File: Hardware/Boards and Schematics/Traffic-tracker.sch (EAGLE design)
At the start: 7 parts, among them J1 POWER_JACK1

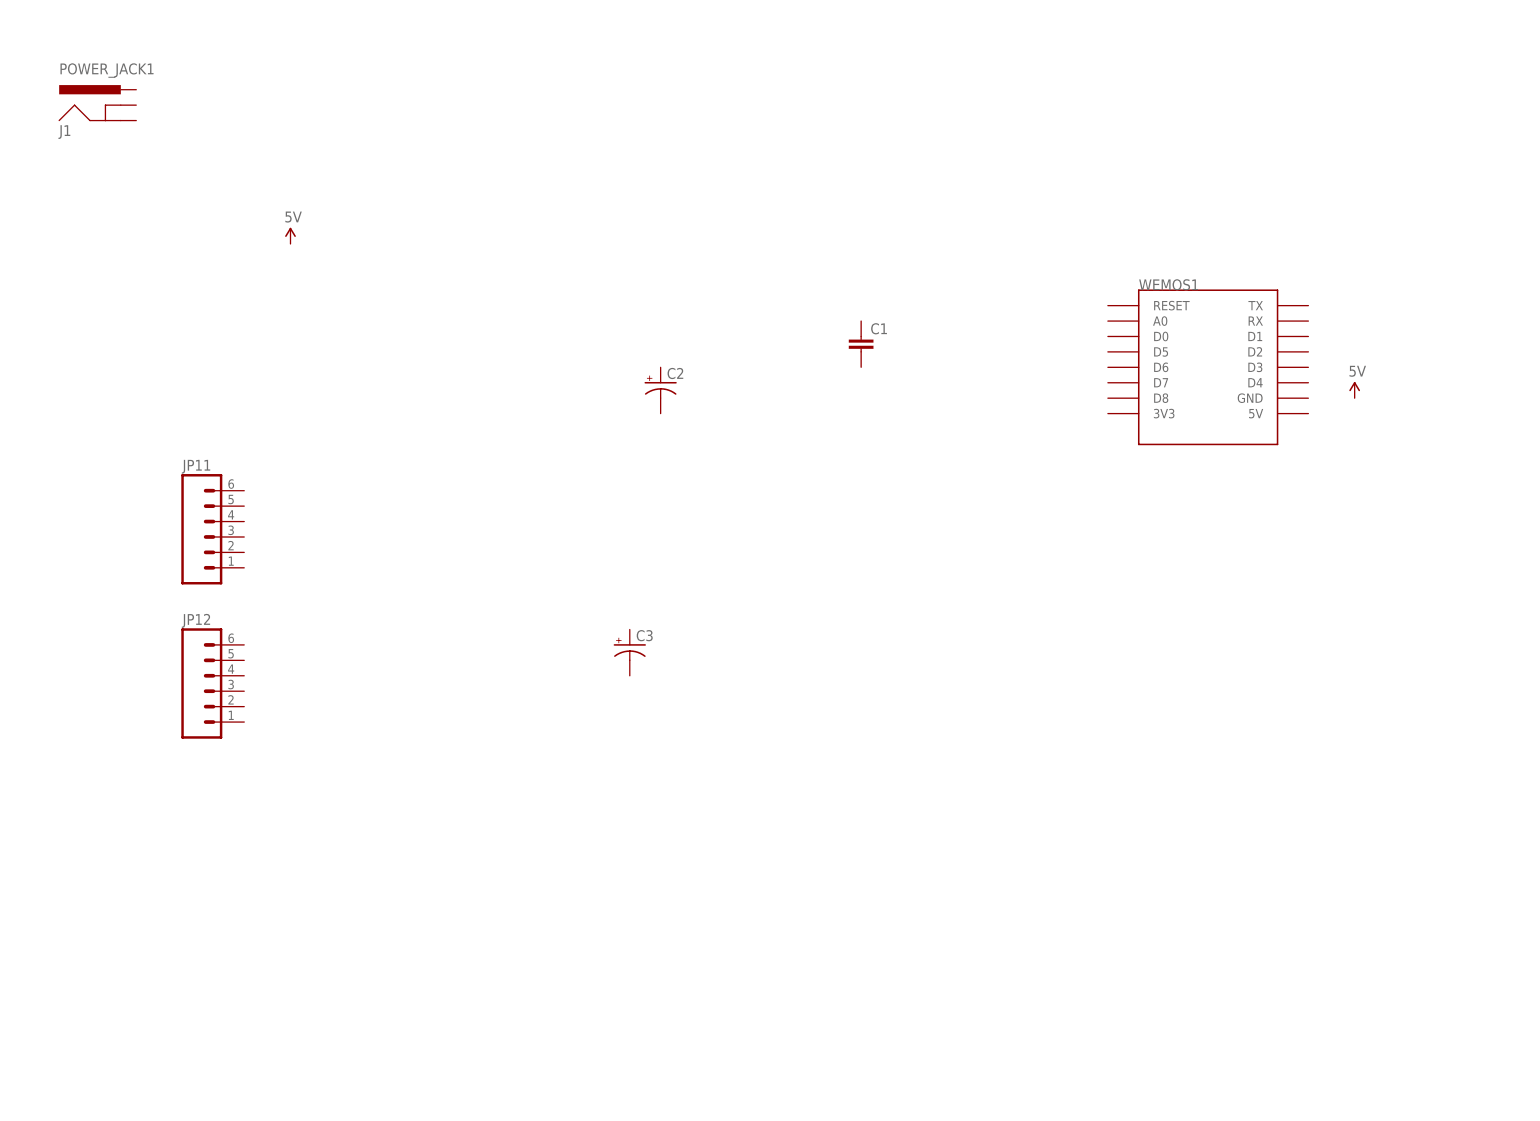
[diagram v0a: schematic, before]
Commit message: Cleaned up schematic, generated and laid out board
Added a 2,2mm barrel jack, 3 pos jumper (for neopixel connection), and
logic level shifter (74AHCT245). Organised schematic neatly.

Board file generated, barrel jack connections double checked, big-ass
trace for 4A connection to neopixels routed. Tried to keep wifi antenna
away from big-ass power traces.

Double checked logic level shifter connections.
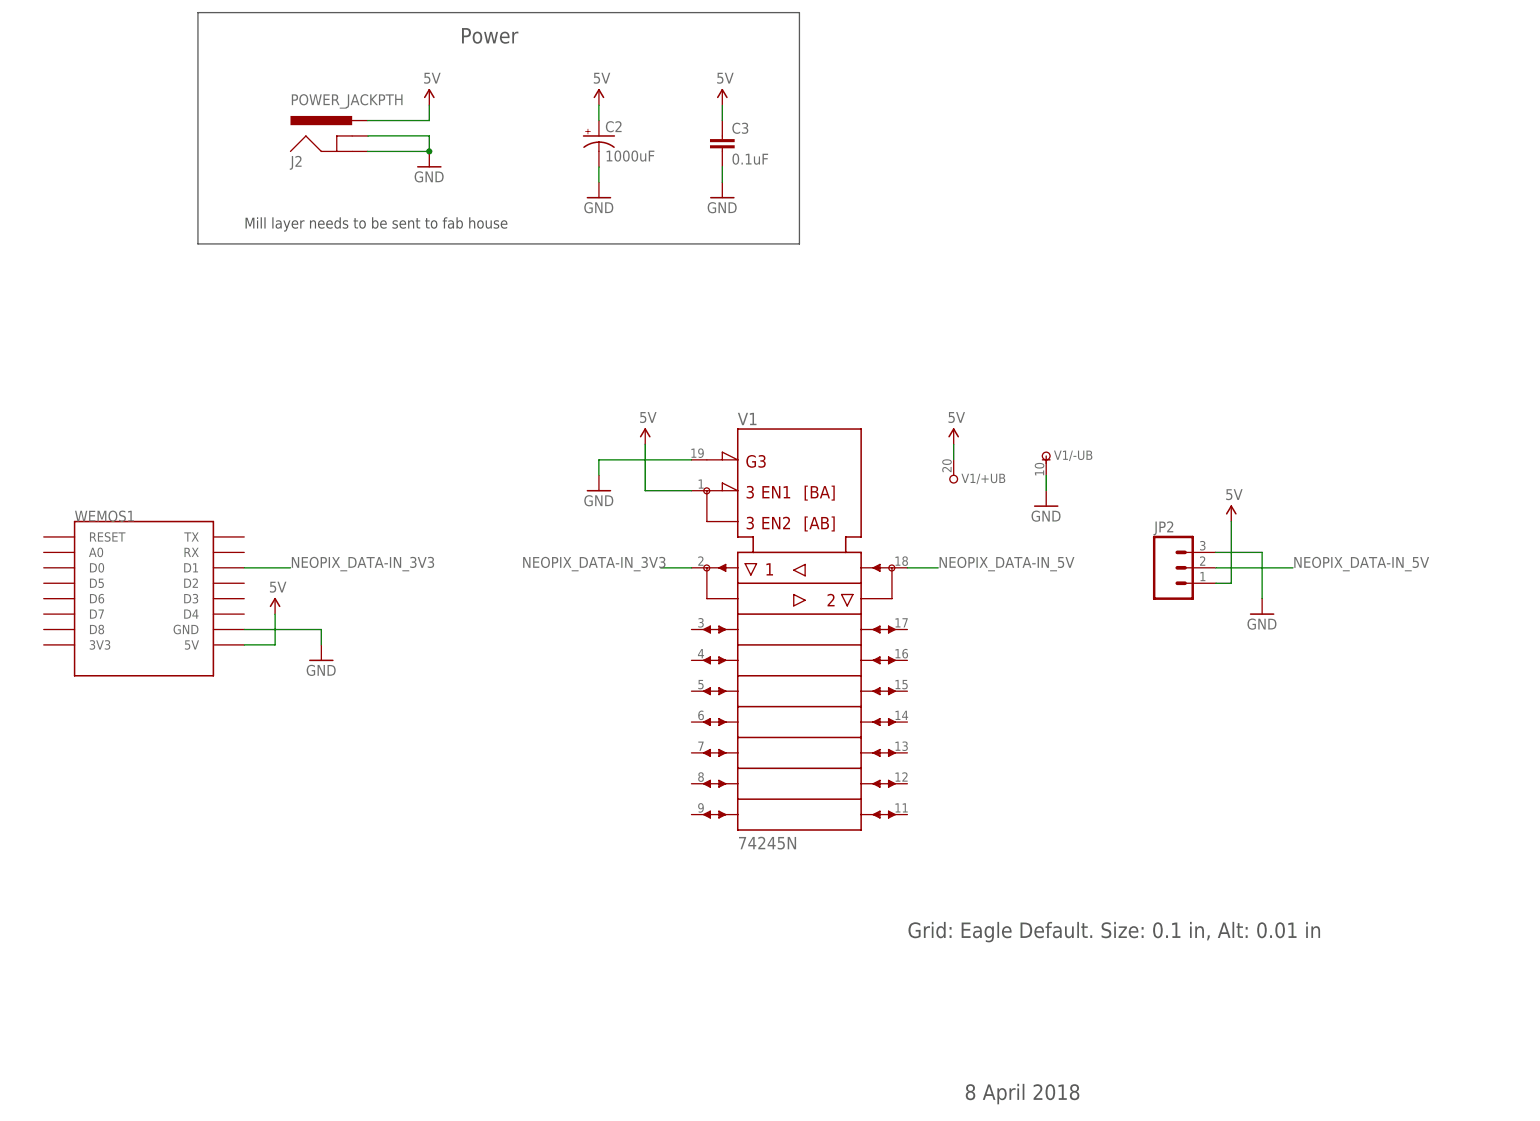
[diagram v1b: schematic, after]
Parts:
- removed C1: (no value), SparkFun:CAP0603-CAP
- removed J1: POWER_JACK1, SparkFun-Connectors:POWER_JACK1
- removed JP11, JP12: (no value), SparkFun-Connectors:M06LOCK
- added J2: POWER_JACKPTH, SparkFun:POWER_JACKPTH
- added JP2: (no value), SparkFun:M03-SCREW-5MM
- added V1: 74245N, 74ttl-din:74245N
- C2: value (none) -> 1000uF
- C3: value (none) -> 0.1uF; device SparkFun-Capacitors:CAP_POLPTH4 -> SparkFun:CAP0603-CAP
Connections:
- new net 5V: C2.+, C3.1, J2.PWR, JP2.1, V1/+UB.+UB, V11.DIR, WEMOS1.5V
- new net GND: C2.-, C3.2, J2.GND, J2.GNDBREAK, JP2.3, V1/-UB.-UB, V11.!G, WEMOS1.GND
- new net NEOPIX_DATA-IN_3V3: V11.A1, WEMOS1.D1
- new net NEOPIX_DATA-IN_5V: JP2.2, V11.B1
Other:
- note added: "8 April 2018"
- note added: "Grid: Eagle Default. Size: 0.1 in, Alt: 0.01 in"
- note added: "Mill layer needs to be sent to fab house"
- note added: "Power"
- moved on the sheet: C2, WEMOS1
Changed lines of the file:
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@@
 <parts>
 <part name="FRAME1" library="frames" deviceset="LETTER_L" device=""/>
-<part name="J1" library="SparkFun-Connectors" deviceset="POWER_JACK" device="1"/>
 <part name="WEMOS1" library="esp8266modules" deviceset="WEMOS-D1-MINI" device=""/>
-<part name="C1" library="SparkFun" deviceset="CAP" device="0603-CAP"/>
-<part name="C2" library="SparkFun-Capacitors" deviceset="CAP_POL" device="PTH4"/>
-<part name="C3" library="SparkFun-Capacitors" deviceset="CAP_POL" device="PTH4"/>
-<part name="JP11" library="SparkFun-Connectors" deviceset="M06" device="LOCK"/>
-<part name="JP12" library="SparkFun-Connectors" deviceset="M06" device="LOCK"/>
+<part name="C2" library="SparkFun-Capacitors" deviceset="CAP_POL" device="PTH4" value="1000uF"/>
 <part name="U$1" library="SparkFun" deviceset="5V" device=""/>
 <part name="U$2" library="SparkFun" deviceset="5V" device=""/>
+<part name="J2" library="SparkFun" deviceset="POWER_JACK" device="PTH"/>
+<part name="GND1" library="SparkFun" deviceset="GND" device=""/>
+<part name="U$4" library="SparkFun" deviceset="5V" device=""/>
+<part name="GND3" library="SparkFun" deviceset="GND" device=""/>
+<part name="GND4" library="SparkFun" deviceset="GND" device=""/>
+<part name="V1" library="74ttl-din" deviceset="74*245" device="N"/>
+<part name="C3" library="SparkFun" deviceset="CAP" device="0603-CAP" value="0.1uF"/>
+<part name="U$5" library="SparkFun" deviceset="5V" device=""/>
+<part name="GND5" library="SparkFun" deviceset="GND" device=""/>
+<part name="U$6" library="SparkFun" deviceset="5V" device=""/>
+<part name="GND6" library="SparkFun" deviceset="GND" device=""/>
+<part name="GND7" library="SparkFun" deviceset="GND" device=""/>
+<part name="U$7" library="SparkFun" deviceset="5V" device=""/>
+<part name="JP2" library="SparkFun" deviceset="M03" device="-SCREW-5MM"/>
+<part name="U$8" library="SparkFun" deviceset="5V" device=""/>
+<part name="GND8" library="SparkFun" deviceset="GND" device=""/>
 </parts>
 <sheets>
 <sheet>
 <plain>
+<text x="40.64" y="144.78" size="1.778" layer="97">Mill layer needs to be sent to fab house</text>
+<wire x1="33.02" y1="180.34" x2="33.02" y2="142.24" width="0.1524" layer="97"/>
+<wire x1="33.02" y1="142.24" x2="132.08" y2="142.24" width="0.1524" layer="97"/>
+<wire x1="132.08" y1="142.24" x2="132.08" y2="180.34" width="0.1524" layer="97"/>
+<wire x1="132.08" y1="180.34" x2="33.02" y2="180.34" width="0.1524" layer="97"/>
+<text x="76.2" y="175.26" size="2.54" layer="97">Power</text>
+<text x="159.258" y="1.27" size="2.54" layer="97">8 April 2018</text>
+<text x="149.86" y="27.94" size="2.54" layer="97">Grid: Eagle Default. Size: 0.1 in, Alt: 0.01 in</text>
 </plain>
 <instances>
 <instance part="FRAME1" gate="G$1" x="0" y="0"/>
-<instance part="FRAME1" gate="G$2" x="147.32" y="0"/>
-<instance part="J1" gate="G$1" x="20.32" y="160.02"/>
-<instance part="WEMOS1" gate="D1" x="198.12" y="121.92"/>
-<instance part="C1" gate="G$1" x="142.24" y="124.46"/>
-<instance part="C2" gate="G$1" x="109.22" y="119.38"/>
-<instance part="C3" gate="G$1" x="104.14" y="76.2"/>
-<instance part="JP11" gate="G$1" x="35.56" y="93.98"/>
-<instance part="JP12" gate="G$1" x="35.56" y="68.58"/>
-<instance part="U$1" gate="G$1" x="223.52" y="116.84"/>
-<instance part="U$2" gate="G$1" x="48.26" y="142.24"/>
+<instance part="FRAME1" gate="G$2" x="147.32" y="0" smashed="yes">
+<attribute name="SHEET" x="233.68" y="1.27" size="2.54" layer="94"/>
+<attribute name="DRAWING_NAME" x="165.1" y="19.05" size="2.54" layer="94"/>
+</instance>
+<instance part="WEMOS1" gate="D1" x="22.86" y="83.82"/>
+<instance part="C2" gate="G$1" x="99.06" y="160.02"/>
+<instance part="U$1" gate="G$1" x="45.72" y="81.28"/>
+<instance part="U$2" gate="G$1" x="71.12" y="165.1"/>
+<instance part="J2" gate="G$1" x="58.42" y="154.94"/>
+<instance part="GND1" gate="1" x="71.12" y="154.94"/>
+<instance part="U$4" gate="G$1" x="99.06" y="165.1"/>
+<instance part="GND3" gate="1" x="99.06" y="149.86"/>
+<instance part="GND4" gate="1" x="53.34" y="73.66"/>
+<instance part="V1" gate="1" x="132.08" y="78.74"/>
+<instance part="C3" gate="G$1" x="119.38" y="157.48"/>
+<instance part="U$5" gate="G$1" x="119.38" y="165.1"/>
+<instance part="GND5" gate="1" x="119.38" y="149.86"/>
+<instance part="V1" gate="/+UB" x="157.48" y="104.14"/>
+<instance part="V1" gate="/-UB" x="172.72" y="106.68"/>
+<instance part="U$6" gate="G$1" x="157.48" y="109.22"/>
+<instance part="GND6" gate="1" x="172.72" y="99.06"/>
+<instance part="GND7" gate="1" x="99.06" y="101.6"/>
+<instance part="U$7" gate="G$1" x="106.68" y="109.22"/>
+<instance part="JP2" gate="G$1" x="193.04" y="88.9"/>
+<instance part="U$8" gate="G$1" x="203.2" y="96.52"/>
+<instance part="GND8" gate="1" x="208.28" y="81.28"/>
 </instances>
 <busses>
 </busses>
 <nets>
+<net name="5V" class="0">
+<segment>
+<pinref part="U$2" gate="G$1" pin="5V"/>
+<wire x1="71.12" y1="165.1" x2="71.12" y2="162.56" width="0.1524" layer="91"/>
+<pinref part="J2" gate="G$1" pin="PWR"/>
+<wire x1="71.12" y1="162.56" x2="60.96" y2="162.56" width="0.1524" layer="91"/>
+</segment>
+<segment>
+<pinref part="U$4" gate="G$1" pin="5V"/>
+<pinref part="C2" gate="G$1" pin="+"/>
+<wire x1="99.06" y1="165.1" x2="99.06" y2="162.56" width="0.1524" layer="91"/>
+</segment>
+<segment>
+<pinref part="U$1" gate="G$1" pin="5V"/>
+<wire x1="45.72" y1="81.28" x2="45.72" y2="76.2" width="0.1524" layer="91"/>
+<pinref part="WEMOS1" gate="D1" pin="5V"/>
+<wire x1="45.72" y1="76.2" x2="40.64" y2="76.2" width="0.1524" layer="91"/>
+</segment>
+<segment>
+<pinref part="U$5" gate="G$1" pin="5V"/>
+<pinref part="C3" gate="G$1" pin="1"/>
+<wire x1="119.38" y1="165.1" x2="119.38" y2="162.56" width="0.1524" layer="91"/>
+</segment>
+<segment>
+<pinref part="U$6" gate="G$1" pin="5V"/>
+<pinref part="V1" gate="/+UB" pin="+UB"/>
+<wire x1="157.48" y1="109.22" x2="157.48" y2="106.68" width="0.1524" layer="91"/>
+</segment>
+<segment>
+<pinref part="U$7" gate="G$1" pin="5V"/>
+<wire x1="106.68" y1="109.22" x2="106.68" y2="101.6" width="0.1524" layer="91"/>
+<pinref part="V1" gate="1" pin="DIR"/>
+<wire x1="106.68" y1="101.6" x2="114.3" y2="101.6" width="0.1524" layer="91"/>
+</segment>
+<segment>
+<pinref part="U$8" gate="G$1" pin="5V"/>
+<wire x1="203.2" y1="96.52" x2="203.2" y2="86.36" width="0.1524" layer="91"/>
+<pinref part="JP2" gate="G$1" pin="1"/>
+<wire x1="203.2" y1="86.36" x2="200.66" y2="86.36" width="0.1524" layer="91"/>
+</segment>
+</net>
+<net name="GND" class="0">
+<segment>
+<pinref part="J2" gate="G$1" pin="GND"/>
+<pinref part="GND1" gate="1" pin="GND"/>
+<wire x1="60.96" y1="157.48" x2="71.12" y2="157.48" width="0.1524" layer="91"/>
+<pinref part="J2" gate="G$1" pin="GNDBREAK"/>
+<wire x1="60.96" y1="160.02" x2="71.12" y2="160.02" width="0.1524" layer="91"/>
+<wire x1="71.12" y1="160.02" x2="71.12" y2="157.48" width="0.1524" layer="91"/>
+<junction x="71.12" y="157.48"/>
+</segment>
+<segment>
+<pinref part="C2" gate="G$1" pin="-"/>
+<pinref part="GND3" gate="1" pin="GND"/>
+<wire x1="99.06" y1="154.94" x2="99.06" y2="152.4" width="0.1524" layer="91"/>
+</segment>
+<segment>
+<pinref part="WEMOS1" gate="D1" pin="GND"/>
+<wire x1="40.64" y1="78.74" x2="53.34" y2="78.74" width="0.1524" layer="91"/>
+<pinref part="GND4" gate="1" pin="GND"/>
+<wire x1="53.34" y1="78.74" x2="53.34" y2="76.2" width="0.1524" layer="91"/>
+</segment>
+<segment>
+<pinref part="C3" gate="G$1" pin="2"/>
+<pinref part="GND5" gate="1" pin="GND"/>
+<wire x1="119.38" y1="154.94" x2="119.38" y2="152.4" width="0.1524" layer="91"/>
+</segment>
+<segment>
+<pinref part="V1" gate="/-UB" pin="-UB"/>
+<pinref part="GND6" gate="1" pin="GND"/>
+<wire x1="172.72" y1="104.14" x2="172.72" y2="101.6" width="0.1524" layer="91"/>
+</segment>
+<segment>
+<pinref part="V1" gate="1" pin="!G"/>
+<pinref part="GND7" gate="1" pin="GND"/>
+<wire x1="114.3" y1="106.68" x2="99.06" y2="106.68" width="0.1524" layer="91"/>
+<wire x1="99.06" y1="106.68" x2="99.06" y2="104.14" width="0.1524" layer="91"/>
+</segment>
+<segment>
+<pinref part="JP2" gate="G$1" pin="3"/>
+<wire x1="200.66" y1="91.44" x2="208.28" y2="91.44" width="0.1524" layer="91"/>
+<pinref part="GND8" gate="1" pin="GND"/>
+<wire x1="208.28" y1="91.44" x2="208.28" y2="83.82" width="0.1524" layer="91"/>
+</segment>
+</net>
+<net name="NEOPIX_DATA-IN_3V3" class="0">
+<segment>
+<pinref part="WEMOS1" gate="D1" pin="D1"/>
+<wire x1="40.64" y1="88.9" x2="48.26" y2="88.9" width="0.1524" layer="91"/>
+<label x="48.26" y="88.9" size="1.778" layer="95"/>
+</segment>
+<segment>
+<pinref part="V1" gate="1" pin="A1"/>
+<wire x1="114.3" y1="88.9" x2="109.22" y2="88.9" width="0.1524" layer="91"/>
+<label x="86.36" y="88.9" size="1.778" layer="95"/>
+</segment>
+</net>
+<net name="NEOPIX_DATA-IN_5V" class="0">
+<segment>
+<pinref part="V1" gate="1" pin="B1"/>
+<wire x1="149.86" y1="88.9" x2="154.94" y2="88.9" width="0.1524" layer="91"/>
+<label x="154.94" y="88.9" size="1.778" layer="95"/>
+</segment>
+<segment>
+<pinref part="JP2" gate="G$1" pin="2"/>
+<wire x1="200.66" y1="88.9" x2="213.36" y2="88.9" width="0.1524" layer="91"/>
+<label x="213.36" y="88.9" size="1.778" layer="95"/>
+</segment>
+</net>
 </nets>
 </sheet>
 </sheets>
+<errors>
+</errors>
 </schematic>
 </drawing>

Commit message: Added protoboard section, cleaned up directory
Protoboard section with rails for 5V, 3v3, GND, and extra holes have
been added.

Trying to remove autosave .brd and .sch files
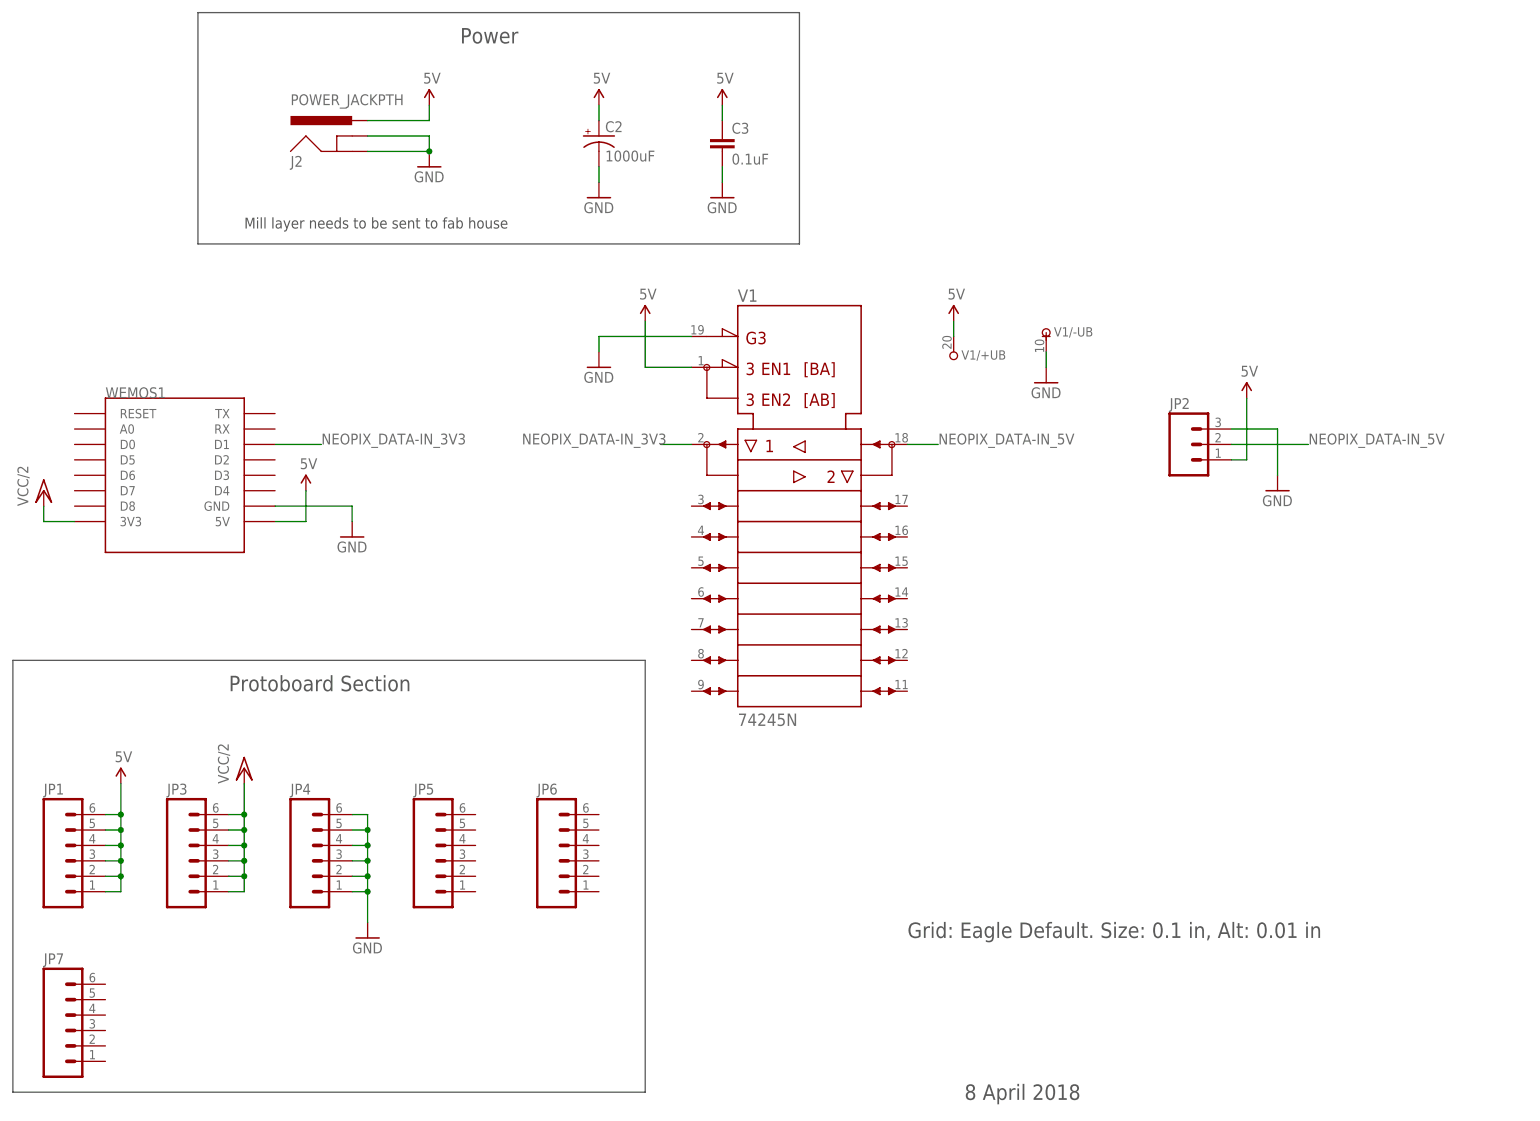
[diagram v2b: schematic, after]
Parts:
- added JP1, JP3, JP4, JP5, JP6, JP7: (no value), SparkFun:M06POGOPIN_HOLES_ONLY
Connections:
- new net VCC/2: JP3.1, JP3.2, JP3.3, JP3.4, JP3.5, JP3.6, WEMOS1.3V3
- net 5V: now also JP1.1, JP1.2, JP1.3, JP1.4, JP1.5, JP1.6
- net GND: now also JP4.1, JP4.2, JP4.3, JP4.4, JP4.5, JP4.6
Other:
- note added: "Protoboard Section"
- moved on the sheet: JP2, V1, V1/+UB, V1/-UB, WEMOS1
